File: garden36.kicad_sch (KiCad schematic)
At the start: 82 parts, among them J1 Conn_01x02, J2 Conn_01x02, SW1 SW_SPDT, SW2 SW_Push, SW3 SW_SPDT, SW4 SW_Push, U1 nice_nano, U2 nice_nano

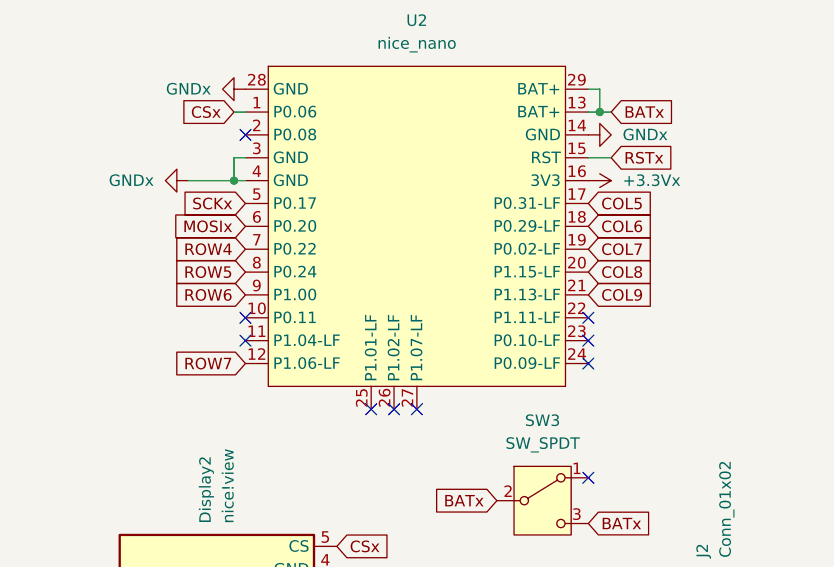
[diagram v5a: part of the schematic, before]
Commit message: Filled zones for both halfs
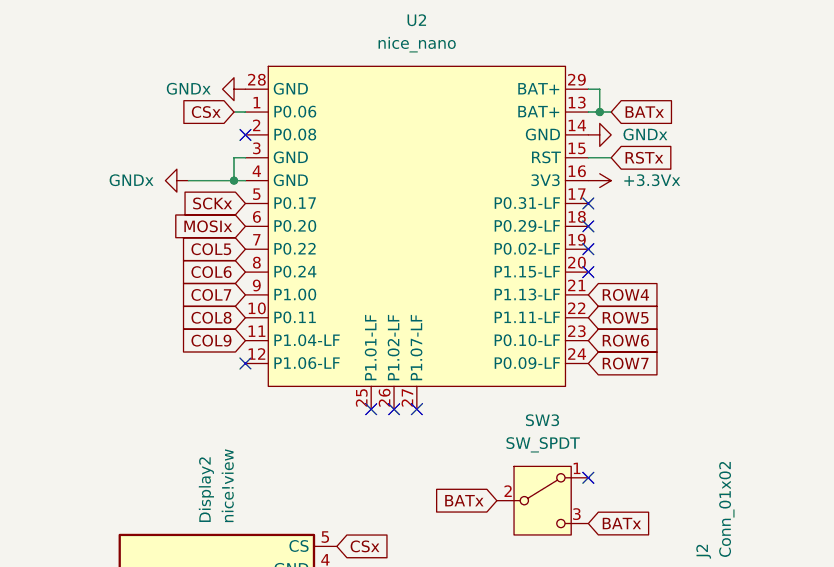
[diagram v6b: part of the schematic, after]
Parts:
- U1, U2: now in the parts list
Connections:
- net COL5: now also U2.7 (P0.22); no longer U2.17 (P0.31-LF)
- net COL6: now also U2.8 (P0.24); no longer U2.18 (P0.29-LF)
- net COL7: now also U2.9 (P1.00); no longer U2.19 (P0.02-LF)
- net COL8: now also U2.10 (P0.11); no longer U2.20 (P1.15-LF)
- net COL9: now also U2.11 (P1.04-LF); no longer U2.21 (P1.13-LF)
- net ROW4: now also U2.21 (P1.13-LF); no longer U2.7 (P0.22)
- net ROW5: now also U2.22 (P1.11-LF); no longer U2.8 (P0.24)
- net ROW6: now also U2.23 (P0.10-LF); no longer U2.9 (P1.00)
- net ROW7: now also U2.24 (P0.09-LF); no longer U2.12 (P1.06-LF)
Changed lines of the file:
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@@
 	)
 	(no_connect
-		(at 116.84 151.13)
+		(at 154.94 146.05)
 	)
 	(no_connect
@@
 	)
 	(no_connect
-		(at 116.84 153.67)
+		(at 154.94 138.43)
 	)
 	(no_connect
@@
 	)
 	(no_connect
-		(at 48.26 160.02)
+		(at 154.94 140.97)
 	)
 	(no_connect
-		(at 135.89 161.29)
+		(at 48.26 160.02)
 	)
 	(no_connect
-		(at 154.94 151.13)
+		(at 135.89 161.29)
 	)
 	(no_connect
-		(at 154.94 156.21)
+		(at 133.35 161.29)
 	)
 	(no_connect
-		(at 133.35 161.29)
+		(at 154.94 143.51)
 	)
 	(no_connect
@@
 	)
 	(no_connect
-		(at 154.94 153.67)
+		(at 116.84 156.21)
 	)
 	(no_connect
@@
 	(global_label "COL5"
 		(shape input)
-		(at 154.94 138.43 0)
+		(at 116.84 143.51 180)
 		(fields_autoplaced yes)
 		(effects
@@
 				(size 1.27 1.27)
 			)
-			(justify left)
+			(justify right)
 		)
 		(property "Intersheetrefs" "${INTERSHEET_REFS}"
-			(at 162.7633 138.43 0)
+			(at 109.0167 143.51 0)
 			(effects
 				(font
 					(size 1.27 1.27)
 				)
-				(justify left)
+				(justify right)
 				(hide yes)
 			)
@@
 	(global_label "ROW4"
 		(shape input)
-		(at 116.84 143.51 180)
+		(at 154.94 148.59 0)
 		(fields_autoplaced yes)
 		(effects
@@
 				(size 1.27 1.27)
 			)
-			(justify right)
+			(justify left)
 		)
 		(property "Intersheetrefs" "${INTERSHEET_REFS}"
-			(at 108.5934 143.51 0)
+			(at 163.1866 148.59 0)
 			(effects
 				(font
 					(size 1.27 1.27)
 				)
-				(justify right)
+				(justify left)
 				(hide yes)
 			)
@@
 	(global_label "COL6"
 		(shape input)
-		(at 154.94 140.97 0)
+		(at 116.84 146.05 180)
 		(fields_autoplaced yes)
 		(effects
@@
 				(size 1.27 1.27)
 			)
-			(justify left)
+			(justify right)
 		)
 		(property "Intersheetrefs" "${INTERSHEET_REFS}"
-			(at 162.7633 140.97 0)
+			(at 109.0167 146.05 0)
 			(effects
 				(font
 					(size 1.27 1.27)
 				)
-				(justify left)
+				(justify right)
 				(hide yes)
 			)
@@
 	(global_label "COL9"
 		(shape input)
-		(at 154.94 148.59 0)
+		(at 116.84 153.67 180)
 		(fields_autoplaced yes)
 		(effects
@@
 				(size 1.27 1.27)
 			)
-			(justify left)
+			(justify right)
 		)
 		(property "Intersheetrefs" "${INTERSHEET_REFS}"
-			(at 162.7633 148.59 0)
+			(at 109.0167 153.67 0)
 			(effects
 				(font
 					(size 1.27 1.27)
 				)
-				(justify left)
+				(justify right)
 				(hide yes)
 			)
@@
 	(global_label "ROW7"
 		(shape input)
-		(at 116.84 156.21 180)
+		(at 154.94 156.21 0)
 		(fields_autoplaced yes)
 		(effects
@@
 				(size 1.27 1.27)
 			)
-			(justify right)
+			(justify left)
 		)
 		(property "Intersheetrefs" "${INTERSHEET_REFS}"
-			(at 108.5934 156.21 0)
+			(at 163.1866 156.21 0)
 			(effects
 				(font
 					(size 1.27 1.27)
 				)
-				(justify right)
+				(justify left)
 				(hide yes)
 			)
@@
 	(global_label "ROW6"
 		(shape input)
-		(at 116.84 148.59 180)
+		(at 154.94 153.67 0)
 		(fields_autoplaced yes)
 		(effects
@@
 				(size 1.27 1.27)
 			)
-			(justify right)
+			(justify left)
 		)
 		(property "Intersheetrefs" "${INTERSHEET_REFS}"
-			(at 108.5934 148.59 0)
+			(at 163.1866 153.67 0)
 			(effects
 				(font
 					(size 1.27 1.27)
 				)
-				(justify right)
+				(justify left)
 				(hide yes)
 			)
@@
 	(global_label "ROW5"
 		(shape input)
-		(at 116.84 146.05 180)
+		(at 154.94 151.13 0)
 		(fields_autoplaced yes)
 		(effects
@@
 				(size 1.27 1.27)
 			)
-			(justify right)
+			(justify left)
 		)
 		(property "Intersheetrefs" "${INTERSHEET_REFS}"
-			(at 108.5934 146.05 0)
+			(at 163.1866 151.13 0)
 			(effects
 				(font
 					(size 1.27 1.27)
 				)
-				(justify right)
+				(justify left)
 				(hide yes)
 			)
@@
 	(global_label "COL7"
 		(shape input)
-		(at 154.94 143.51 0)
+		(at 116.84 148.59 180)
 		(fields_autoplaced yes)
 		(effects
@@
 				(size 1.27 1.27)
 			)
-			(justify left)
+			(justify right)
 		)
 		(property "Intersheetrefs" "${INTERSHEET_REFS}"
-			(at 162.7633 143.51 0)
+			(at 109.0167 148.59 0)
 			(effects
 				(font
 					(size 1.27 1.27)
 				)
-				(justify left)
+				(justify right)
 				(hide yes)
 			)
@@
 	(global_label "COL8"
 		(shape input)
-		(at 154.94 146.05 0)
+		(at 116.84 151.13 180)
 		(fields_autoplaced yes)
 		(effects
@@
 				(size 1.27 1.27)
 			)
-			(justify left)
+			(justify right)
 		)
 		(property "Intersheetrefs" "${INTERSHEET_REFS}"
-			(at 162.7633 146.05 0)
+			(at 109.0167 151.13 0)
 			(effects
 				(font
 					(size 1.27 1.27)
 				)
-				(justify left)
+				(justify right)
 				(hide yes)
 			)
@@
 		(unit 1)
 		(exclude_from_sim no)
-		(in_bom no)
+		(in_bom yes)
 		(on_board yes)
 		(dnp no)
@@
 		(unit 1)
 		(exclude_from_sim no)
-		(in_bom no)
+		(in_bom yes)
 		(on_board yes)
 		(dnp no)

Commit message: V1 ordered
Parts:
- J1, J2: footprint PCM_marbastlib-various:CON_JST_ACH_BM02B -> Connector_JST:JST_PH_S2B-PH-K_1x02_P2.00mm_Horizontal

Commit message: V2 started
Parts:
- U1, U2: now left out of the parts list
- renumbered CH22 to CH20, CH25 to CH21, CH29 to CH22, CH33 to CH23, CH20 to CH24, CH23 to CH25, CH30 to CH27, CH34 to CH28, CH21 to CH29, CH24 to CH30, CH27 to CH31, CH31 to CH32, CH35 to CH33, CH28 to CH34, CH32 to CH35, D22 to D20, D25 to D21, D29 to D22, D33 to D23, D20 to D24, D23 to D25, D30 to D27, D34 to D28, D21 to D29, D24 to D30, D27 to D31, D31 to D32, D35 to D33, D28 to D34, D32 to D35
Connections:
- net BAT: no longer SW1.3 (C), U1.13 (BAT+), U1.29 (BAT+)
- net COL0: no longer U1.17 (P0.31-LF)
- net COL1: no longer U1.18 (P0.29-LF)
- net COL2: no longer U1.19 (P0.02-LF)
- net COL3: no longer U1.20 (P1.15-LF)
- net COL4: no longer U1.21 (P1.13-LF)
- net GND: no longer U1.28 (GND)
- net MOSI: now also U1.5 (P0.17); no longer U1.6 (P0.20)
- net ROW0: no longer U1.7 (P0.22)
- net ROW1: no longer U1.8 (P0.24)
- net ROW2: no longer U1.9 (P1.00)
- net ROW3: no longer U1.12 (P1.06-LF)
- net SCK: now also U1.6 (P0.20); no longer U1.5 (P0.17)
- net +3.3Vx renamed R_+3.3V
- removed net BATx: J2.1 (Pin_1), SW3.2 (B), SW3.3 (C), U2.13 (BAT+), U2.29 (BAT+)
- net COL5 renamed R_COL0
- net R_COL0: now also CH34.1; no longer U2.7 (P0.22)
- net COL6 renamed R_COL1
- net R_COL1: now also CH35.1; no longer U2.8 (P0.24)
- net COL7 renamed R_COL2
- net R_COL2: now also CH36.1; no longer CH34.1, U2.9 (P1.00)
- net COL8 renamed R_COL3
- net R_COL3: no longer CH35.1, U2.10 (P0.11)
- net COL9 renamed R_COL4
- net R_COL4: no longer CH36.1, U2.11 (P1.04-LF)
- net CSx renamed R_CS
- net GNDx renamed R_GND
- net R_GND: no longer U2.28 (GND)
- net MOSIx renamed R_MOSI
- net R_MOSI: now also U2.5 (P0.17); no longer U2.6 (P0.20)
- net ROW4 renamed R_ROW0
- net R_ROW0: no longer U2.21 (P1.13-LF)
- net ROW5 renamed R_ROW1
- net R_ROW1: no longer U2.22 (P1.11-LF)
- net ROW6 renamed R_ROW2
- net R_ROW2: no longer U2.23 (P0.10-LF)
- net ROW7 renamed R_ROW3
- net R_ROW3: no longer U2.24 (P0.09-LF)
- net RSTx renamed R_RST
- net SCKx renamed R_SCK
- net R_SCK: now also U2.6 (P0.20); no longer U2.5 (P0.17)
- new net B+: U1.29 (BAT+)
- new net B-: U1.28 (GND)
- new net RAW: SW1.3 (C), U1.13 (BAT+)
- new net R_B+: U2.29 (BAT+)
- new net R_B-: U2.28 (GND)
- new net R_BAT: J2.1 (Pin_1), SW3.2 (B)
- new net R_RAW: SW3.3 (C), U2.13 (BAT+)
- no-connect marks 20 -> 2
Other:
- moved on the sheet: CH1, CH10, CH11, CH12, CH13, CH14, CH15, CH16, CH17, CH18, CH19, CH2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
